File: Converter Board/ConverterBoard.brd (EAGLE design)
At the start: 101.6 x 101.6 mm, 17 parts

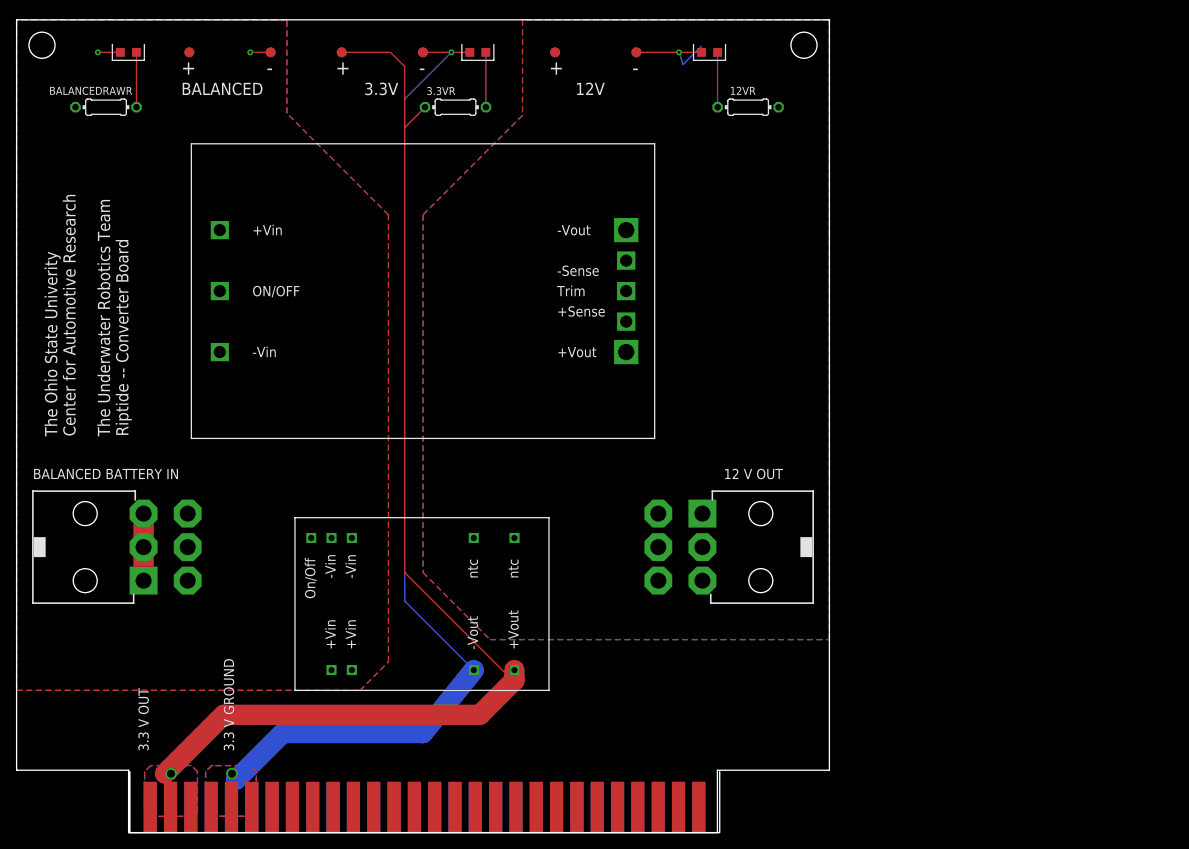
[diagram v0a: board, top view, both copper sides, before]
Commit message: Fixed 3.3V converter Added extra connector Updated board with new parts
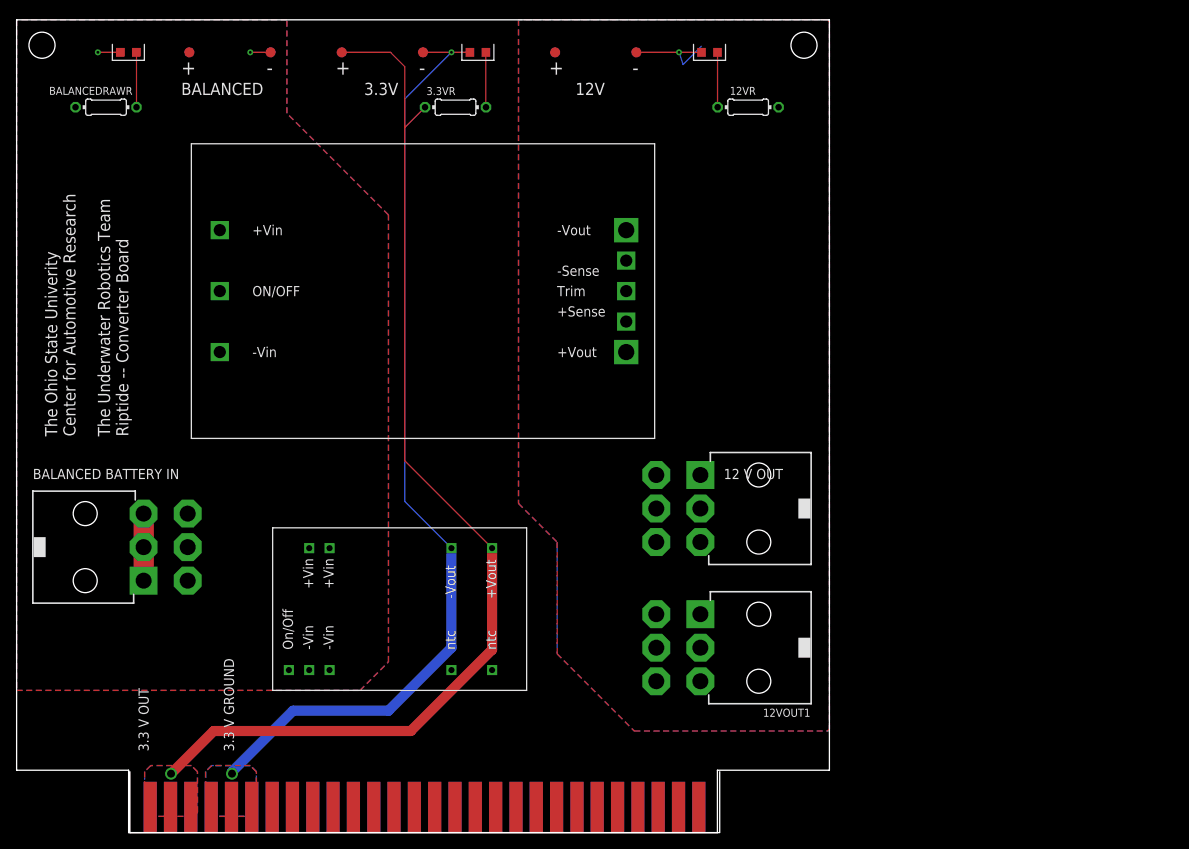
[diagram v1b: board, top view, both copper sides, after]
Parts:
- added 12VOUT1: 39-30-06?, con-molex-mini-fit:39-30-?06?
- moved 12VOUT 4.83 mm to (85.5, 40.5)
- moved U$2 2.79 mm to (63.8, 17.8)
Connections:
- net 12V+: now also 12VOUT1.1, 12VOUT1.2, 12VOUT1.3
- net 12V-: now also 12VOUT1.4, 12VOUT1.5, 12VOUT1.6
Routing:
- net 3.3V: track 144.2 -> 136.2 mm
- net 3.3VGROUND: track 125.0 -> 119.2 mm
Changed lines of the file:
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@@
 <element name="U$3" library="5530843-6" package="5530843-6-BOARDFINGERS" value="5530843" x="15.875" y="0"/>
 <element name="BALANCEDRAWIN" library="con-molex-mini-fit" package="39-30-?06?" value="39-30-06?" x="15.875" y="35.6875" smashed="yes" rot="R270"/>
-<element name="12VOUT" library="con-molex-mini-fit" package="39-30-?06?" value="39-30-06?" x="85.725" y="35.6875" smashed="yes" rot="R90"/>
+<element name="12VOUT" library="con-molex-mini-fit" package="39-30-?06?" value="39-30-06?" x="85.471" y="40.5135" smashed="yes" rot="R90"/>
 <element name="U$1" library="12VCONV" package="12VCONV" value="12VCONV" x="21.844" y="49.276"/>
-<element name="U$2" library="3.3V Converter" package="3.3VCONV" value="3.3VCONV" x="66.548" y="17.78" rot="R90"/>
 <element name="3.3VLED" library="LTST-S270GKT" package="LTST-S270GKT" value="LTST-S270GKT" x="57.658" y="97.536"/>
 <element name="12VLED" library="LTST-S270GKT" package="LTST-S270GKT" value="LTST-S270GKT" x="86.614" y="97.536"/>
@@
 <attribute name="VALUE" x="50.165" y="96.774" size="0.0254" layer="27"/>
 </element>
+<element name="U$2" library="3.3V Converter" package="3.3VCONV" value="3.3VCONV" x="63.754" y="17.78" rot="R90"/>
+<element name="12VOUT1" library="con-molex-mini-fit" package="39-30-?06?" value="39-30-06?" x="85.471" y="23.114" rot="R90"/>
 </elements>
 <signals>
@@
 <contactref element="BALANCEDRAWIN" pad="2"/>
 <contactref element="BALANCEDRAWIN" pad="1"/>
-<contactref element="U$2" pad="22"/>
-<contactref element="U$2" pad="23"/>
 <wire x1="15.875" y1="35.6875" x2="15.875" y2="39.8785" width="2.54" layer="1"/>
 <wire x1="15.875" y1="35.6875" x2="15.875" y2="31.4965" width="2.54" layer="1"/>
@@
 <vertex x="33.782" y="101.6"/>
 </polygon>
+<contactref element="U$2" pad="23"/>
+<contactref element="U$2" pad="22"/>
 </signal>
 <signal name="BALANCEDRAW-">
@@
 <contactref element="BALANCEDRAWIN" pad="4"/>
 <contactref element="U$1" pad="3,-VIN"/>
-<contactref element="U$2" pad="2"/>
-<contactref element="U$2" pad="3"/>
 <contactref element="BALANCEDRAWLED" pad="CATHODE"/>
 <via x="10.16" y="97.536" extent="1-16" drill="0.35"/>
@@
 </polygon>
 <wire x1="10.16" y1="97.536" x2="12.97" y2="97.536" width="0.1524" layer="1"/>
+<contactref element="U$2" pad="2"/>
+<contactref element="U$2" pad="3"/>
 </signal>
 <signal name="12V-">
@@
 <contactref element="12VOUT" pad="5"/>
 <contactref element="12VLED" pad="CATHODE"/>
-<polygon width="0.1524" layer="16">
-<vertex x="63.246" y="101.6"/>
-<vertex x="63.246" y="89.662"/>
-<vertex x="50.8" y="77.216"/>
-<vertex x="50.8" y="32.512"/>
-<vertex x="59.182" y="24.13"/>
-<vertex x="101.6" y="24.13"/>
-<vertex x="101.6" y="101.6"/>
-</polygon>
 <via x="82.804" y="97.536" extent="1-16" drill="0.35"/>
 <wire x1="82.804" y1="97.536" x2="83.312" y2="96.012" width="0.1524" layer="16"/>
@@
 <wire x1="77.47" y1="97.536" x2="82.804" y2="97.536" width="0.1524" layer="1"/>
 <wire x1="82.804" y1="97.536" x2="85.614" y2="97.536" width="0.1524" layer="1"/>
+<contactref element="12VOUT1" pad="4"/>
+<contactref element="12VOUT1" pad="6"/>
+<contactref element="12VOUT1" pad="5"/>
+<polygon width="0.1524" layer="16">
+<vertex x="62.738" y="101.6"/>
+<vertex x="62.738" y="41.148"/>
+<vertex x="67.564" y="36.322"/>
+<vertex x="67.564" y="35.814"/>
+<vertex x="67.564" y="22.352"/>
+<vertex x="77.216" y="12.7"/>
+<vertex x="101.6" y="12.7"/>
+<vertex x="101.6" y="101.6"/>
+</polygon>
 </signal>
 <signal name="3.3V">
@@
 </polygon>
 <via x="19.304" y="7.366" extent="1-16" drill="1"/>
-<contactref element="U$2" pad="14"/>
 <contactref element="3.3VR" pad="2"/>
-<wire x1="62.23" y1="19.05" x2="62.23" y2="20.32" width="2.54" layer="1"/>
-<wire x1="62.23" y1="19.05" x2="57.912" y2="14.732" width="2.54" layer="1"/>
-<wire x1="57.912" y1="14.732" x2="25.908" y2="14.732" width="2.54" layer="1"/>
-<wire x1="25.908" y1="14.732" x2="18.542" y2="7.366" width="2.54" layer="1"/>
-<wire x1="48.514" y1="32.512" x2="48.514" y2="88.138" width="0.1524" layer="1"/>
 <wire x1="48.514" y1="88.138" x2="51.054" y2="90.678" width="0.1524" layer="1"/>
 <contactref element="3.3VTP" pad="TP"/>
@@
 <wire x1="48.514" y1="95.758" x2="46.736" y2="97.536" width="0.1524" layer="1"/>
 <wire x1="46.736" y1="97.536" x2="40.64" y2="97.536" width="0.1524" layer="1"/>
-<wire x1="62.23" y1="20.32" x2="61.976" y2="20.066" width="0.1524" layer="1"/>
-<wire x1="61.976" y1="20.066" x2="60.96" y2="20.066" width="0.1524" layer="1"/>
-<wire x1="60.96" y1="20.066" x2="48.514" y2="32.512" width="0.1524" layer="1"/>
+<contactref element="U$2" pad="14"/>
+<wire x1="59.436" y1="22.86" x2="59.436" y2="35.56" width="1.27" layer="1"/>
+<wire x1="59.436" y1="22.86" x2="49.276" y2="12.7" width="1.27" layer="1"/>
+<wire x1="49.276" y1="12.7" x2="24.638" y2="12.7" width="1.27" layer="1"/>
+<wire x1="24.638" y1="12.7" x2="19.304" y2="7.366" width="1.27" layer="1"/>
+<wire x1="59.436" y1="35.56" x2="48.514" y2="46.482" width="0.1524" layer="1"/>
+<wire x1="48.514" y1="46.482" x2="48.514" y2="88.138" width="0.1524" layer="1"/>
 </signal>
 <signal name="3.3VGROUND">
@@
 <vertex x="23.622" y="7.62"/>
 </polygon>
-<contactref element="U$2" pad="16"/>
 <polygon width="0.3048" layer="16" thermals="no">
 <vertex x="24.384" y="8.382"/>
@@
 <vertex x="29.21" y="8.382"/>
 </polygon>
-<wire x1="50.8" y1="12.446" x2="57.15" y2="20.32" width="2.54" layer="16"/>
-<wire x1="50.8" y1="12.446" x2="33.274" y2="12.446" width="2.54" layer="16"/>
-<wire x1="33.274" y1="12.446" x2="27.432" y2="6.604" width="2.54" layer="16"/>
 <via x="26.924" y="7.366" extent="1-16" drill="1"/>
 <contactref element="3.3VLED" pad="CATHODE"/>
@@
 <contactref element="3.3VGROUNDTP" pad="TP"/>
 <wire x1="54.356" y1="97.536" x2="50.8" y2="97.536" width="0.1524" layer="1"/>
-<wire x1="57.15" y1="20.32" x2="48.514" y2="28.956" width="0.1524" layer="16"/>
 <wire x1="48.514" y1="91.694" x2="54.356" y2="97.536" width="0.1524" layer="16"/>
-<wire x1="48.514" y1="28.956" x2="48.514" y2="91.694" width="0.1524" layer="16"/>
+<contactref element="U$2" pad="16"/>
+<wire x1="54.356" y1="23.114" x2="54.356" y2="35.56" width="1.27" layer="16"/>
+<wire x1="54.356" y1="23.114" x2="46.482" y2="15.24" width="1.27" layer="16"/>
+<wire x1="46.482" y1="15.24" x2="34.544" y2="15.24" width="1.27" layer="16"/>
+<wire x1="34.544" y1="15.24" x2="26.924" y2="7.62" width="1.27" layer="16"/>
+<wire x1="26.924" y1="7.62" x2="26.924" y2="7.366" width="1.27" layer="16"/>
+<wire x1="54.356" y1="35.56" x2="48.514" y2="41.402" width="0.1524" layer="16"/>
+<wire x1="48.514" y1="41.402" x2="48.514" y2="91.694" width="0.1524" layer="16"/>
 </signal>
 <signal name="12V+">
 <contactref element="U$1" pad="8,+VOUT"/>
-<polygon width="0.1524" layer="1">
-<vertex x="63.246" y="101.6"/>
-<vertex x="63.246" y="89.662"/>
-<vertex x="50.8" y="77.216"/>
-<vertex x="50.8" y="32.512"/>
-<vertex x="59.182" y="24.13"/>
-<vertex x="101.6" y="24.13"/>
-<vertex x="101.6" y="101.6"/>
-</polygon>
 <contactref element="12VOUT" pad="3"/>
 <contactref element="12VOUT" pad="1"/>
@@
 <contactref element="12VR" pad="2"/>
 <contactref element="12V+TP" pad="TP"/>
+<contactref element="12VOUT1" pad="2"/>
+<contactref element="12VOUT1" pad="1"/>
+<contactref element="12VOUT1" pad="3"/>
+<polygon width="0.1524" layer="1">
+<vertex x="62.738" y="101.6"/>
+<vertex x="62.738" y="41.148"/>
+<vertex x="67.564" y="36.322"/>
+<vertex x="67.564" y="22.352"/>
+<vertex x="77.216" y="12.7"/>
+<vertex x="101.346" y="12.7"/>
+<vertex x="101.6" y="12.954"/>
+<vertex x="101.6" y="101.346"/>
+<vertex x="101.346" y="101.6"/>
+</polygon>
 </signal>
 <signal name="3.3VLED">

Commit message: Cleaned and updated converter board, added spots for capacitors
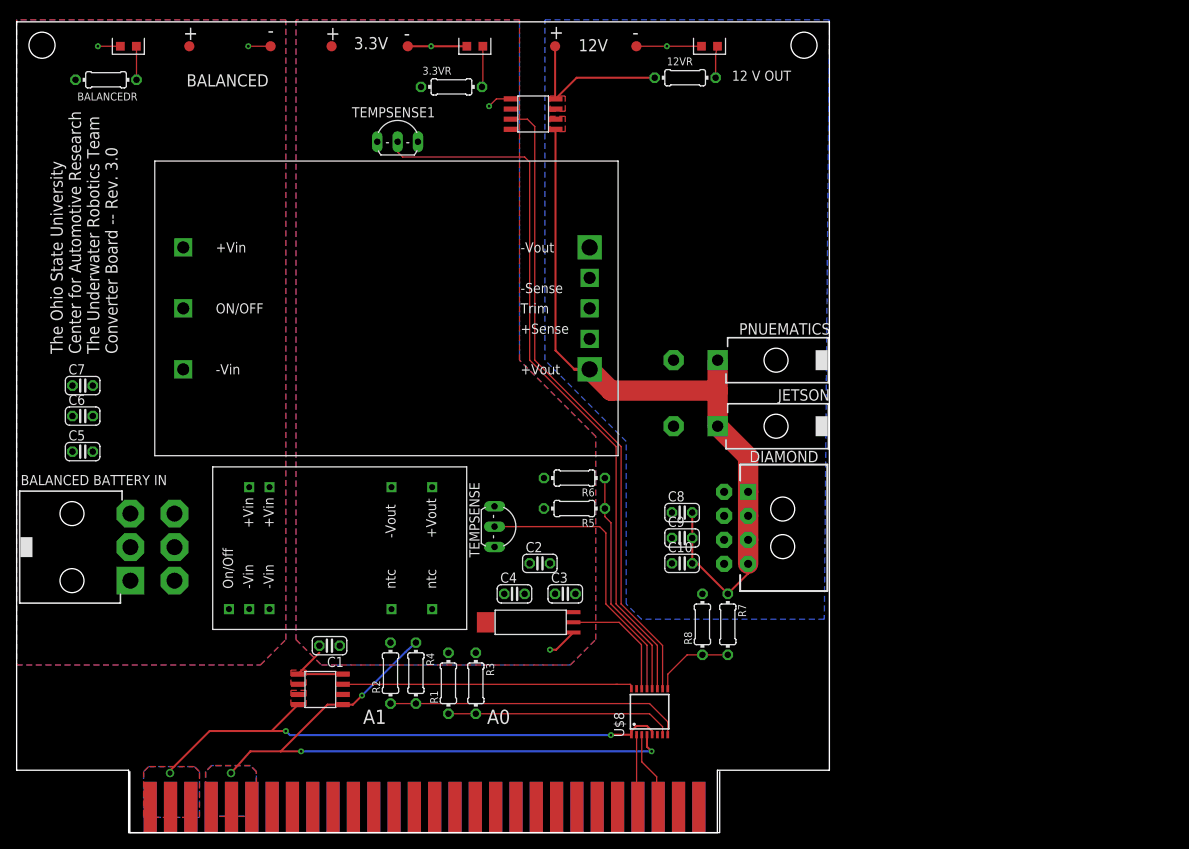
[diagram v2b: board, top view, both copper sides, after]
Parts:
- removed 12V-TP1, 3.3VGROUNDTP, 3.3VTP, BALANCEDRAW+TP, BALANCEDRAW-TP: PTR1B1,27, testpad:B1,27
- removed 12VOUT, 12VOUT1: 39-30-06?, con-molex-mini-fit:39-30-?06?
- removed BALANCEDRAWLED: LTST-S270GKT, LTST-S270GKT:LTST-S270GKT
- removed BALANCEDRAWR: 700, resistor:0204/7
- removed U$1: 12VCONV, 12VCONV:12VCONV
- added 12V-TP, 3.3V+TP, 3.3V-TP, BALANCED+TP, BALANCED-TP: PTR1B1,27, testpad:B1,27
- added 12VCONVERTER: 12VCONV, 12VCONV:12VCONV
- added 12VCURRENT, 3.3VCURRENT: CURRENTSENS, CurrentSensor:CURRENTSENS
- added BALANCEDLED: LTST-S270GKT, LTST-S270GKT:LTST-S270GKT
- added BALANCEDR: 700, resistor:0204/7
- added C1: 0.1 uF, resistor:C025-024X044
- added C10, C2, C3, C4, C5, C6, C7, C8, C9: (no value), resistor:C025-024X044
- added DIAMOND: 43045-08, con-molex-micro-fit:43045-08
- added JETSON, PNUEMATICS: 39-30-02?, con-molex-mini-fit:39-30-?02?
- added R1, R2, R3, R4, R5, R6, R7, R8: (no value), resistor:0204/7
- added TEMPSENSE, TEMPSENSE1: 2SC458, transistor:TO92-ECB
- added U$6: HUMIDITYSENSOR, HumiditySensor:HUMIDITYSENSOR
- added U$8: ADC128D818, ADC128D818:TSSOP-16
- moved U$2 10.7 mm to (56.3, 25.4)
- moved 12VR 8.69 mm to (83.6, 94.4)
- moved 3.3VR 2.59 mm to (54.4, 93.2)
- moved BALANCEDRAWIN 1.65 mm to (14.2, 35.7)
- moved 3.3VLED 0.85 mm to (57.3, 98.3)
- moved 12V+TP 0.76 mm to (67.3, 98.3)
- moved 12VLED 0.76 mm to (86.6, 98.3)
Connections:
- removed net 12V+: 12V+TP.TP, 12VOUT.1, 12VOUT.2, 12VOUT.3, 12VOUT1.1, 12VOUT1.2, 12VOUT1.3, 12VR.2, U$1.8,+VOUT
- removed net 12V-: 12V-TP1.TP, 12VLED.CATHODE, 12VOUT.4, 12VOUT.5, 12VOUT.6, 12VOUT1.4, 12VOUT1.5, 12VOUT1.6, U$1.4,-VOUT
- removed net 3.3V: 3.3VR.2, 3.3VTP.TP, U$2.14, U$3.3.3VP1, U$3.3.3VP2, U$3.3.3VP3, U$3.3.3V_4, U$3.3.3V_5, U$3.3.3V_6
- removed net 3.3VGROUND: 3.3VGROUNDTP.TP, 3.3VLED.CATHODE, U$2.16, U$3.GND1, U$3.GND2, U$3.GND3, U$3.GND_4, U$3.GND_5, U$3.GND_6
- removed net BALANCEDRAW+: BALANCEDRAW+TP.TP, BALANCEDRAWIN.1, BALANCEDRAWIN.2, BALANCEDRAWIN.3, BALANCEDRAWR.1, U$1.1,+VIN, U$1.2,ON/OFF, U$2.22, U$2.23
- removed net BALANCEDRAW-: BALANCEDRAW-TP.TP, BALANCEDRAWIN.4, BALANCEDRAWIN.5, BALANCEDRAWIN.6, BALANCEDRAWLED.CATHODE, U$1.3,-VIN, U$2.2, U$2.3
- removed net BALANCEDRAWLED: BALANCEDRAWLED.ANODE, BALANCEDRAWR.2
- new net 12IDATA: 12VCURRENT.7,VIOUT, U$8.IN6
- new net 12VDATA: R7.2, R8.1, U$8.IN7
- new net 12VGND: 12V-TP.TP, 12VCONVERTER.4,-VOUT, 12VLED.CATHODE, C10.1, C8.1, C9.1, DIAMOND.5, DIAMOND.6, DIAMOND.7, DIAMOND.8, JETSON.2, PNUEMATICS.2, R8.2
- new net 12VMON: 12V+TP.TP, 12VCURRENT.3,IP-, 12VCURRENT.4,IP-, 12VR.1
- new net 12VUNMON: 12VCONVERTER.8,+VOUT, 12VCURRENT.1,IP+, 12VCURRENT.2,IP+, C10.2, C8.2, C9.2, DIAMOND.1, DIAMOND.2, DIAMOND.3, DIAMOND.4, JETSON.1, PNUEMATICS.1, R7.1
- new net 3.3IDATA: 3.3VCURRENT.7,VIOUT, U$8.IN0
- new net 3.3V+: 12VCURRENT.8,VCC, 3.3V+TP.TP, 3.3VCURRENT.1,IP+, 3.3VCURRENT.2,IP+, 3.3VCURRENT.8,VCC, 3.3VR.2, C1.2, C2.2, C3.2, C4.2, R1.2, R2.2, R6.2, TEMPSENSE.E, TEMPSENSE1.E, U$2.14, U$6.+VE
- new net 3.3VDATA: R5.1, R6.1, U$8.IN4
- new net 3.3VGND: 12VCURRENT.5,GND, 3.3V-TP.TP, 3.3VCURRENT.5,GND, 3.3VLED.CATHODE, C1.1, C2.1, C3.1, C4.1, R3.1, R4.1, R5.2, TEMPSENSE.B, TEMPSENSE1.B, U$2.16, U$3.GND1, U$3.GND2, U$3.GND3, U$3.GND_4, U$3.GND_5, U$3.GND_6, U$6.-VE, U$8.GND
- new net A0: R1.1, R3.2, U$8.A0
- new net A1: R2.1, R4.2, U$8.A1
- new net BALANCED+: 12VCONVERTER.1,+VIN, 12VCONVERTER.2,ON/OFF, BALANCED+TP.TP, BALANCEDR.2, BALANCEDRAWIN.4, BALANCEDRAWIN.5, BALANCEDRAWIN.6, C5.2, C6.2, C7.2, U$2.22, U$2.23
- new net BALANCEDGND: 12VCONVERTER.3,-VIN, BALANCED-TP.TP, BALANCEDLED.CATHODE, BALANCEDRAWIN.1, BALANCEDRAWIN.2, BALANCEDRAWIN.3, C5.1, C6.1, C7.1, U$2.1, U$2.2, U$2.3
- new net BALANCEDLED: BALANCEDLED.ANODE, BALANCEDR.1
- new net HUMIDITYDATA: U$6.OUT, U$8.IN2
- new net SCL: U$3.SCL_SENSOR, U$8.SCL
- new net SDA: U$3.SDA_SENSOR, U$8.SDA
- new net TEMP1DATA: TEMPSENSE1.C, U$8.IN5
- new net TEMPDATA: TEMPSENSE.C, U$8.IN3
- new net VCC: 3.3VCURRENT.3,IP-, 3.3VCURRENT.4,IP-, U$3.3.3VP1, U$3.3.3VP2, U$3.3.3VP3, U$3.3.3V_4, U$3.3.3V_5, U$3.3.3V_6, U$8.V+, U$8.VREF
- net 12VLED: now also 12VR.2; no longer 12VR.1
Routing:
- net 3.3V: track 136.2 -> 0.00 mm, vias 1 -> 0
- net 3.3VGROUND: track 119.2 -> 0.00 mm, vias 2 -> 0
- net 12VUNMON: track 0.00 -> 94.2 mm
- net 3.3VGND: track 0.00 -> 93.4 mm, vias 0 -> 7
- net TEMP1DATA: track 0.00 -> 90.7 mm
- net 12IDATA: track 0.00 -> 80.3 mm
- net VCC: track 0.00 -> 69.0 mm, vias 0 -> 3
- net A1: track 0.00 -> 37.2 mm
- net 3.3IDATA: track 0.00 -> 36.1 mm
- net TEMPDATA: track 0.00 -> 35.8 mm
- net 3.3VDATA: track 0.00 -> 28.8 mm
- net A0: track 0.00 -> 28.4 mm
- net 12VMON: track 0.00 -> 20.1 mm
- net HUMIDITYDATA: track 0.00 -> 15.2 mm
- net 12V-: track 13.0 -> 0.00 mm, vias 1 -> 0
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- added copper zone on layer 16, net 12VGND
- added copper zone on layer 1, net 12VMON
- added copper zone on layer 1, net 12VUNMON
- added copper zone on layer 1, net 3.3V+
- added copper zone on layer 1, net 3.3VBKPLN
- added copper zone on layer 1, net 3.3VGND
- added copper zone on layer 16, net 3.3VGND
- added copper zone on layer 1, net BALANCED+
- added copper zone on layer 16, net BALANCEDGND
- added copper zone on layer 1, net VCC
- added copper zone on layer 16, net VCC
- removed copper zone on layer 1, net 12V+
- removed copper zone on layer 16, net 12V-
- removed copper zone on layer 1, net 3.3V
- removed copper zone on layer 16, net 3.3V
- removed copper zone on layer 1, net 3.3VGROUND
- removed copper zone on layer 16, net 3.3VGROUND
- removed copper zone on layer 1, net BALANCEDRAW+
- removed copper zone on layer 16, net BALANCEDRAW-
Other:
- board size 101.6 x 101.6 mm -> 101.6 x 101.3 mm
- board text added: "A0"
- board text added: "A1"
- board text added: "The Ohio State University Center for Automotive Research The Underwater Robotics Team Converter Board -- Rev. 3.0"
- board text removed: "3.3 V GROUND"
- board text removed: "3.3 V OUT"
- board text removed: "The Ohio State Univerity Center for Automotive Research"
- board text removed: "The Underwater Robotics Team Riptide -- Converter Board"
